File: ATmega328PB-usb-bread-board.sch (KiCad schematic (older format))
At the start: 32 parts, among them J1 Conn_01x17, J2 Conn_01x17, J3 USB_B_Micro, J4 AVR-ISP-6, J5 Grove-I2C-connector, J6 Grove-I2C-connector, J7 Grove-I2C-connector, U1 ATmega328PB-MU, U2 CP2102N-A01-GQFN28, U3 LMV358

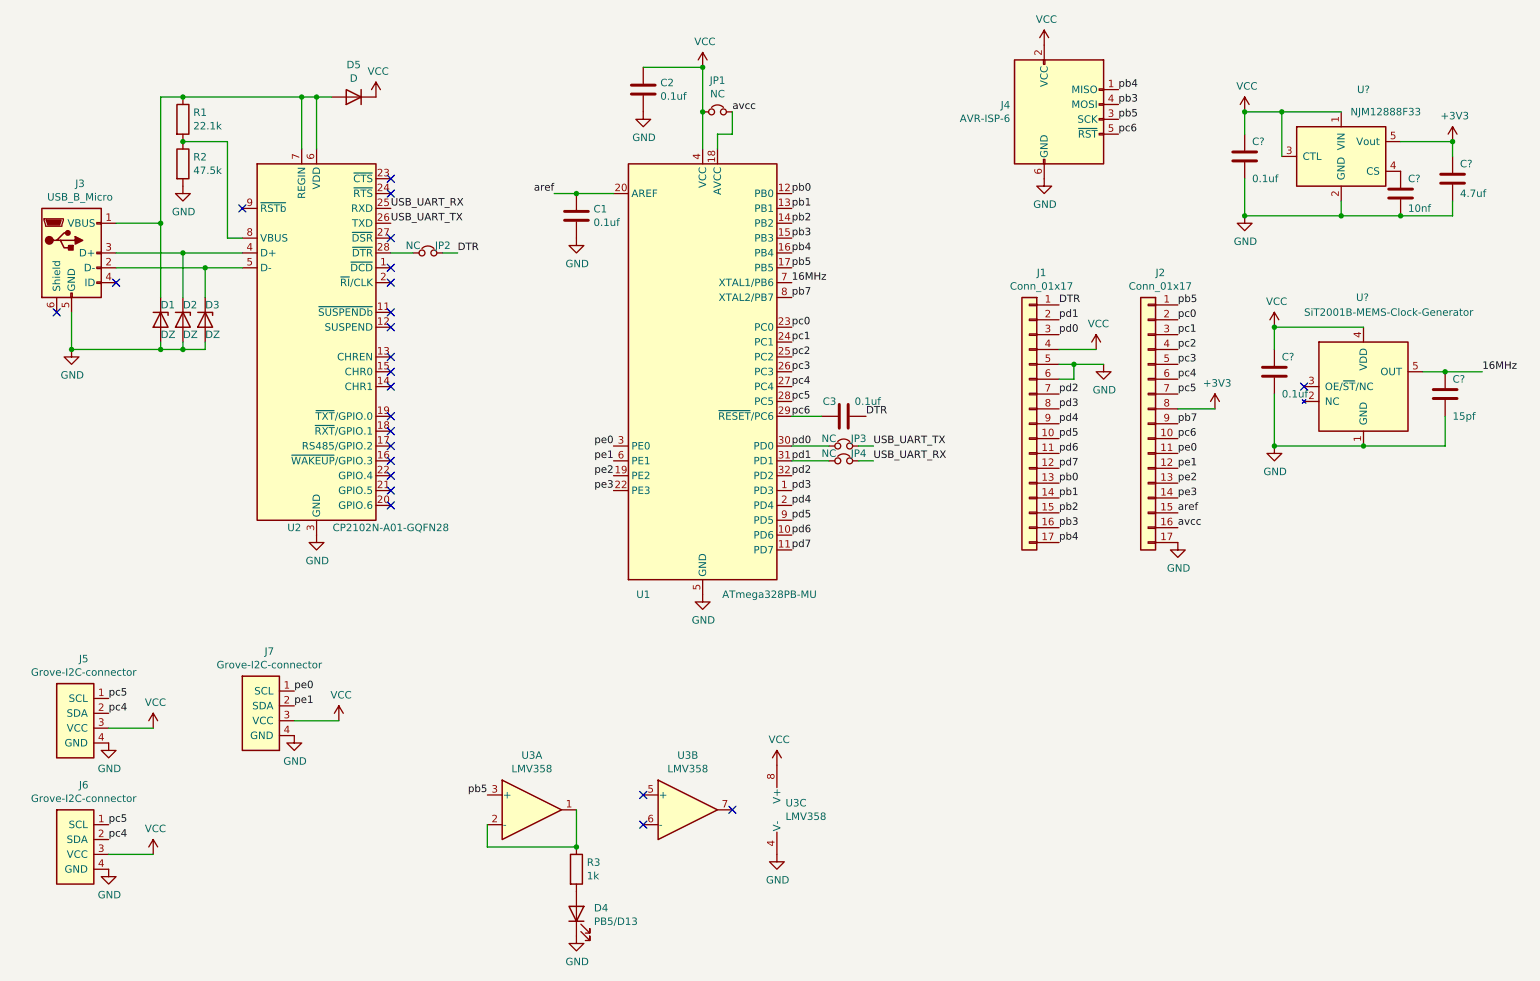
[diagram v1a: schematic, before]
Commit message: Add pullup resister and condensors for cp2102n
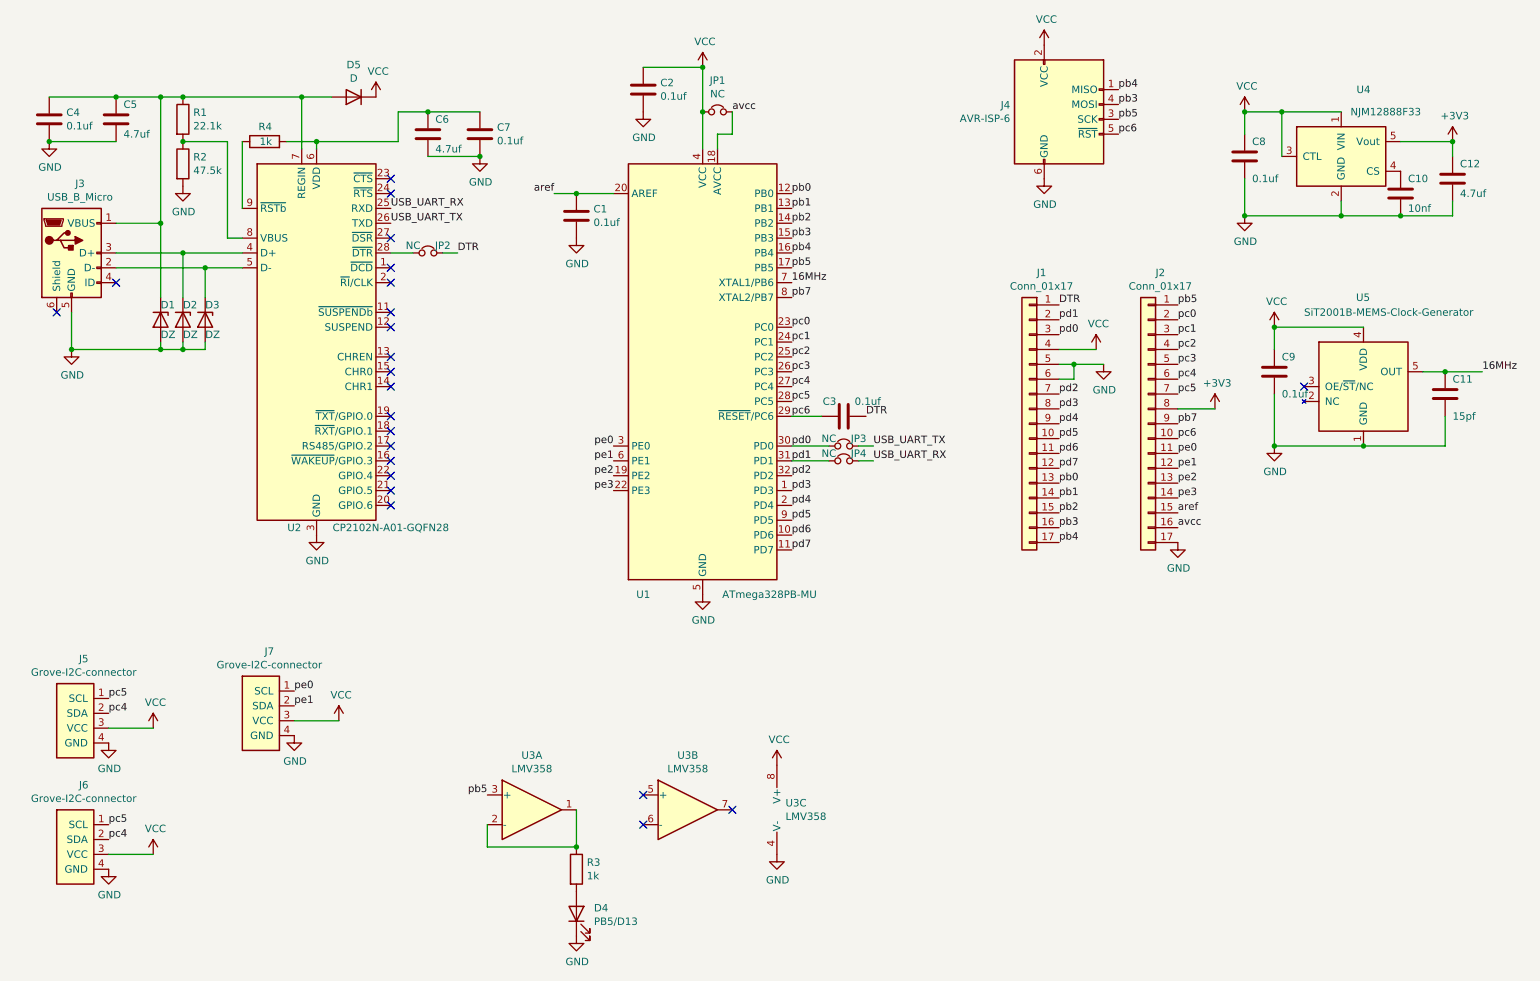
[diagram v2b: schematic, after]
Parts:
- added C4, C7: 0.1uf, Capacitor_SMD:C_0603_1608Metric, symbol Device:C
- added C5, C6: 4.7uf, Capacitor_SMD:C_0402_1005Metric, symbol Device:C
- added R4: 1k, Resistor_SMD:R_0603_1608Metric, symbol Device:R
- gave numbers to parts that had none: 7
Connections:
- net GND: now also C4.2, C5.2, C6.2, C7.2
- net at D1.1 (K), D5.2 (A), J3.1 (VBUS)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: now also C4.1, C5.1; no longer U2.6 (VDD)
- net at U2.9 (~RSTb): now also R4.1
- new net: C6.1, C7.1, R4.2, U2.6 (VDD)
- no-connect marks 24 -> 23
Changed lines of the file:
@@
 	3800 2450 3900 2450
 NoConn ~ 1600 2650
-NoConn ~ 2450 2150
 $Comp
 L power:GND #PWR0110
@@
 	1    0    0    -1
 $EndComp
-Wire Wire Line
-	3050 1400 2950 1400
 Connection ~ 2850 1400
-Wire Wire Line
-	2950 1400 2950 1750
-Connection ~ 2950 1400
-Wire Wire Line
-	2950 1400 2850 1400
-$Comp
-L my-kicad-symbols:NJM12888F33 U?
+$Comp
+L my-kicad-symbols:NJM12888F33 U4
 U 1 1 5F8C64C1
 P 9850 1800
-F 0 "U?" H 10000 2250 50  0000 C CNN
+F 0 "U4" H 10000 2250 50  0000 C CNN
 F 1 "NJM12888F33" H 10150 2100 50  0000 C CNN
 F 2 "Package_TO_SOT_SMD:SOT-23-5" H 9850 1800 50  0001 C CNN
@@
 $EndComp
 $Comp
-L power:VCC #PWR?
+L power:VCC #PWR0111
 U 1 1 5F8C761A
 P 9200 1500
-F 0 "#PWR?" H 9200 1350 50  0001 C CNN
+F 0 "#PWR0111" H 9200 1350 50  0001 C CNN
 F 1 "VCC" H 9215 1673 50  0000 C CNN
 F 2 "" H 9200 1500 50  0001 C CNN
@@
 $EndComp
 $Comp
-L power:GND #PWR?
+L power:GND #PWR0124
 U 1 1 5F8C7AD0
 P 9200 2200
-F 0 "#PWR?" H 9200 1950 50  0001 C CNN
+F 0 "#PWR0124" H 9200 1950 50  0001 C CNN
 F 1 "GND" H 9205 2027 50  0000 C CNN
 F 2 "" H 9200 2200 50  0001 C CNN
@@
 $EndComp
 $Comp
-L Device:C C?
+L Device:C C8
 U 1 1 5F8C87B4
 P 9200 1800
-F 0 "C?" H 9250 1900 50  0000 L CNN
+F 0 "C8" H 9250 1900 50  0000 L CNN
 F 1 "0.1uf" H 9250 1650 50  0000 L CNN
 F 2 "Capacitor_SMD:C_0603_1608Metric" H 9238 1650 50  0001 C CNN
@@
 Connection ~ 9200 1500
 $Comp
-L Device:C C?
+L Device:C C10
 U 1 1 5F8D0B51
 P 10250 2050
-F 0 "C?" H 10300 2150 50  0000 L CNN
+F 0 "C10" H 10300 2150 50  0000 L CNN
 F 1 "10nf" H 10300 1950 50  0000 L CNN
 F 2 "Capacitor_SMD:C_0603_1608Metric" H 10288 1900 50  0001 C CNN
@@
 	9850 2200 10250 2200
 $Comp
-L Device:C C?
+L Device:C C12
 U 1 1 5F8D5F68
 P 10600 1950
-F 0 "C?" H 10650 2050 50  0000 L CNN
+F 0 "C12" H 10650 2050 50  0000 L CNN
 F 1 "4.7uf" H 10650 1850 50  0000 L CNN
 F 2 "Capacitor_SMD:C_0402_1005Metric" H 10638 1800 50  0001 C CNN
@@
 $EndComp
 $Comp
-L power:+3V3 #PWR?
+L power:+3V3 #PWR0125
 U 1 1 5F8D6BD8
 P 10600 1700
-F 0 "#PWR?" H 10600 1550 50  0001 C CNN
+F 0 "#PWR0125" H 10600 1550 50  0001 C CNN
 F 1 "+3V3" H 10615 1873 50  0000 C CNN
 F 2 "" H 10600 1700 50  0001 C CNN
@@
 Connection ~ 10250 2200
 $Comp
-L power:+3V3 #PWR?
+L power:+3V3 #PWR0126
 U 1 1 5F8DE3AD
 P 9000 3500
-F 0 "#PWR?" H 9000 3350 50  0001 C CNN
+F 0 "#PWR0126" H 9000 3350 50  0001 C CNN
 F 1 "+3V3" H 9015 3673 50  0000 C CNN
 F 2 "" H 9000 3500 50  0001 C CNN
@@
 	9000 3500 8750 3500
 $Comp
-L my-kicad-symbols:SiT2001B-MEMS-Clock-Generator U?
+L my-kicad-symbols:SiT2001B-MEMS-Clock-Generator U5
 U 1 1 5F8E3D90
 P 10000 3350
-F 0 "U?" H 9950 3950 50  0000 L CNN
+F 0 "U5" H 9950 3950 50  0000 L CNN
 F 1 "SiT2001B-MEMS-Clock-Generator" H 9600 3850 50  0000 L CNN
 F 2 "" H 10000 3350 50  0001 C CNN
@@
 $EndComp
 $Comp
-L power:VCC #PWR?
+L power:VCC #PWR0127
 U 1 1 5F8E86D4
 P 9400 2950
-F 0 "#PWR?" H 9400 2800 50  0001 C CNN
+F 0 "#PWR0127" H 9400 2800 50  0001 C CNN
 F 1 "VCC" H 9415 3123 50  0000 C CNN
 F 2 "" H 9400 2950 50  0001 C CNN
@@
 $EndComp
 $Comp
-L power:GND #PWR?
+L power:GND #PWR0128
 U 1 1 5F8E86DA
 P 9400 3750
-F 0 "#PWR?" H 9400 3500 50  0001 C CNN
+F 0 "#PWR0128" H 9400 3500 50  0001 C CNN
 F 1 "GND" H 9405 3577 50  0000 C CNN
 F 2 "" H 9400 3750 50  0001 C CNN
@@
 $EndComp
 $Comp
-L Device:C C?
+L Device:C C9
 U 1 1 5F8E86E0
 P 9400 3250
-F 0 "C?" H 9450 3350 50  0000 L CNN
+F 0 "C9" H 9450 3350 50  0000 L CNN
 F 1 "0.1uf" H 9450 3100 50  0000 L CNN
 F 2 "Capacitor_SMD:C_0603_1608Metric" H 9438 3100 50  0001 C CNN
@@
 	9400 2950 10000 2950
 $Comp
-L Device:C C?
+L Device:C C11
 U 1 1 5F8F13DA
 P 10550 3400
-F 0 "C?" H 10600 3500 50  0000 L CNN
+F 0 "C11" H 10600 3500 50  0000 L CNN
 F 1 "15pf" H 10600 3250 50  0000 L CNN
 F 2 "Capacitor_SMD:C_0603_1608Metric" H 10588 3250 50  0001 C CNN
@@
 16MHz
 NoConn ~ 9600 3350
+Wire Wire Line
+	2850 1400 3050 1400
+$Comp
+L Device:R R4
+U 1 1 5F8F4536
+P 2600 1700
+F 0 "R4" V 2700 1650 50  0000 L CNN
+F 1 "1k" V 2600 1650 50  0000 L CNN
+F 2 "Resistor_SMD:R_0603_1608Metric" V 2530 1700 50  0001 C CNN
+F 3 "~" H 2600 1700 50  0001 C CNN
+	1    2600 1700
+	0    -1   -1   0
+$EndComp
+Wire Wire Line
+	2450 1700 2450 2150
+Wire Wire Line
+	2750 1700 2950 1700
+Wire Wire Line
+	2950 1700 2950 1750
+$Comp
+L Device:C C5
+U 1 1 5F8FC33B
+P 1600 1550
+F 0 "C5" H 1650 1650 50  0000 L CNN
+F 1 "4.7uf" H 1650 1450 50  0000 L CNN
+F 2 "Capacitor_SMD:C_0402_1005Metric" H 1638 1400 50  0001 C CNN
+F 3 "~" H 1600 1550 50  0001 C CNN
+	1    1600 1550
+	1    0    0    -1
+$EndComp
+$Comp
+L Device:C C4
+U 1 1 5F9005EE
+P 1150 1550
+F 0 "C4" H 1265 1596 50  0000 L CNN
+F 1 "0.1uf" H 1265 1505 50  0000 L CNN
+F 2 "Capacitor_SMD:C_0603_1608Metric" H 1188 1400 50  0001 C CNN
+F 3 "~" H 1150 1550 50  0001 C CNN
+	1    1150 1550
+	1    0    0    -1
+$EndComp
+$Comp
+L power:GND #PWR0129
+U 1 1 5F9017BB
+P 1150 1700
+F 0 "#PWR0129" H 1150 1450 50  0001 C CNN
+F 1 "GND" H 1155 1527 50  0000 C CNN
+F 2 "" H 1150 1700 50  0001 C CNN
+F 3 "" H 1150 1700 50  0001 C CNN
+	1    1150 1700
+	1    0    0    -1
+$EndComp
+Wire Wire Line
+	1150 1700 1600 1700
+Connection ~ 1150 1700
+Wire Wire Line
+	1900 1400 1600 1400
+Connection ~ 1900 1400
+Connection ~ 1600 1400
+Wire Wire Line
+	1600 1400 1150 1400
+$Comp
+L Device:C C6
+U 1 1 5F9065CD
+P 3700 1650
+F 0 "C6" H 3750 1750 50  0000 L CNN
+F 1 "4.7uf" H 3750 1550 50  0000 L CNN
+F 2 "Capacitor_SMD:C_0402_1005Metric" H 3738 1500 50  0001 C CNN
+F 3 "~" H 3700 1650 50  0001 C CNN
+	1    3700 1650
+	1    0    0    -1
+$EndComp
+$Comp
+L Device:C C7
+U 1 1 5F906DB1
+P 4050 1650
+F 0 "C7" H 4165 1696 50  0000 L CNN
+F 1 "0.1uf" H 4165 1605 50  0000 L CNN
+F 2 "Capacitor_SMD:C_0603_1608Metric" H 4088 1500 50  0001 C CNN
+F 3 "~" H 4050 1650 50  0001 C CNN
+	1    4050 1650
+	1    0    0    -1
+$EndComp
+$Comp
+L power:GND #PWR0130
+U 1 1 5F90741A
+P 4050 1800
+F 0 "#PWR0130" H 4050 1550 50  0001 C CNN
+F 1 "GND" H 4055 1627 50  0000 C CNN
+F 2 "" H 4050 1800 50  0001 C CNN
+F 3 "" H 4050 1800 50  0001 C CNN
+	1    4050 1800
+	1    0    0    -1
+$EndComp
+Wire Wire Line
+	4050 1800 3700 1800
+Connection ~ 4050 1800
+Wire Wire Line
+	2950 1700 3500 1700
+Wire Wire Line
+	3500 1700 3500 1500
+Wire Wire Line
+	3500 1500 3700 1500
+Connection ~ 2950 1700
+Connection ~ 3700 1500
+Wire Wire Line
+	3700 1500 4050 1500
 $EndSCHEMATC
